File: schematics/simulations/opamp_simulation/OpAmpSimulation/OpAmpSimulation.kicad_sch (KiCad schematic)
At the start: 9 parts, among them U1 ${SIM.PARAMS}

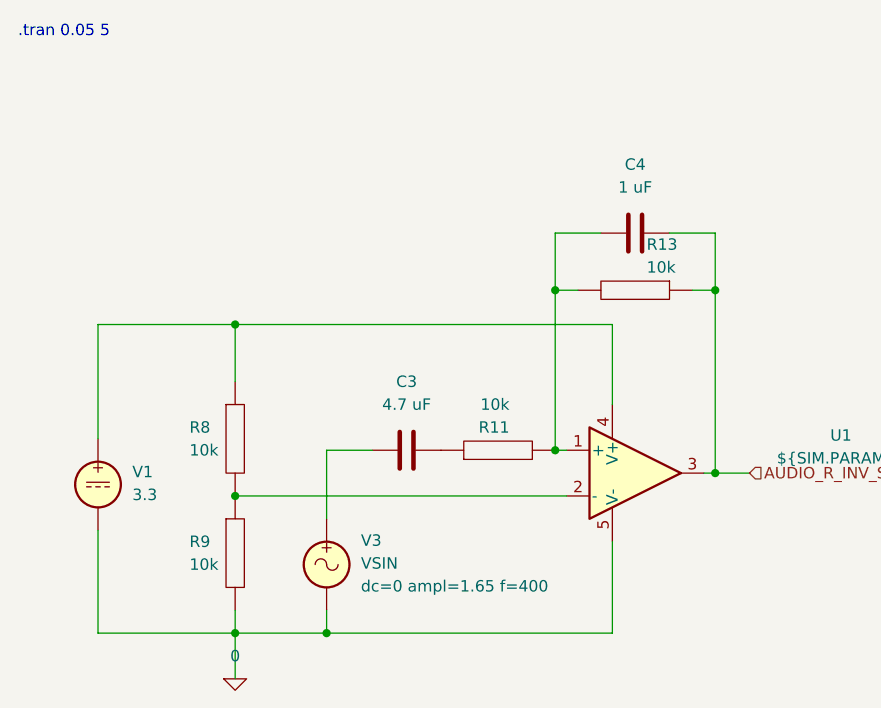
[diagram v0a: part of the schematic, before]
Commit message: [opamp_simulation:*] Bug | Confused inverting / non-inverting input
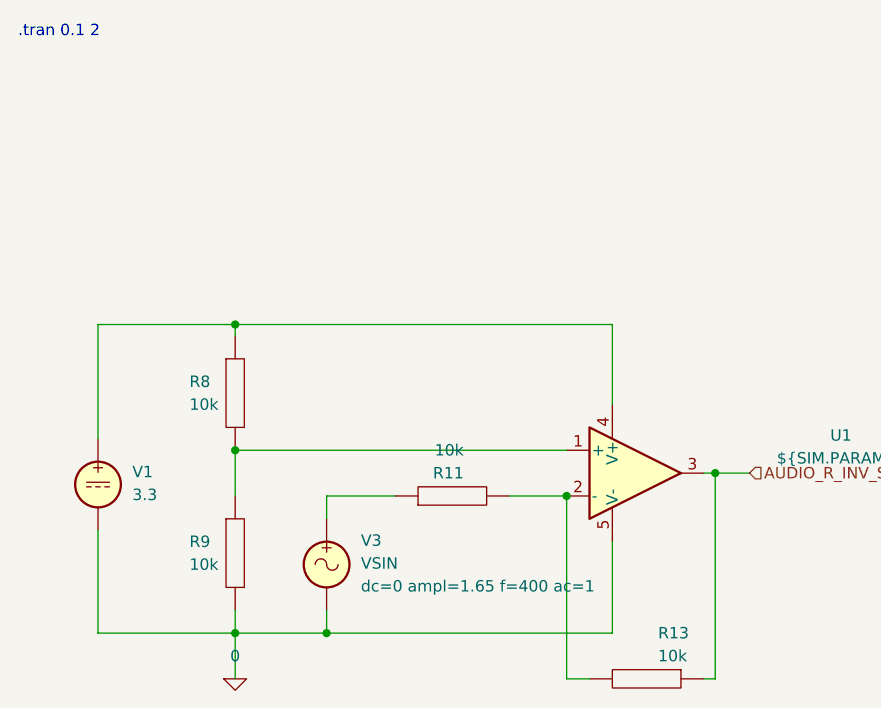
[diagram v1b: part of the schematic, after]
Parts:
- removed C3: 4.7 uF, symbol Device:C
- removed C4: 1 uF, symbol Device:C
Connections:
- net at V3.1: now also R11.1
- net at R11.2, R13.2: now also U1.2 (-); no longer U1.1 (+)
- net at R8.2, R9.1: now also U1.1 (+); no longer U1.2 (-)
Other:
- note added: ".tran 0.1 2"
- note removed: ".tran 0.05 5"
- moved on the sheet: R11, R13, R8
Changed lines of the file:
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@@
   (junction (at 68.58 166.37) (diameter 0) (color 0 0 0 0)
   )
-  (junction (at 93.98 128.27) (diameter 0) (color 0 0 0 0)
-  )
-  (junction (at 111.76 128.27) (diameter 0) (color 0 0 0 0)
-  )
-  (junction (at 93.98 146.05) (diameter 0) (color 0 0 0 0)
-  )
-  (junction (at 58.42 151.13) (diameter 0) (color 0 0 0 0)
+  (junction (at 58.42 146.05) (diameter 0) (color 0 0 0 0)
+  )
+  (junction (at 95.25 151.13) (diameter 0) (color 0 0 0 0)
   )
   (junction (at 58.42 132.08) (diameter 0) (color 0 0 0 0)
@@
   (junction (at 111.76 148.59) (diameter 0) (color 0 0 0 0)
   )
-  (wire (pts (xy 68.58 153.67) (xy 68.58 146.05))
+  (wire (pts (xy 68.58 153.67) (xy 68.58 151.13))
     (stroke (width 0) (type default))
   )
@@
     (stroke (width 0) (type default))
   )
-  (wire (pts (xy 111.76 128.27) (xy 111.76 148.59))
+  (wire (pts (xy 111.76 171.45) (xy 111.76 148.59))
     (stroke (width 0) (type default))
   )
@@
     (stroke (width 0) (type default))
   )
-  (wire (pts (xy 58.42 132.08) (xy 58.42 138.43))
+  (wire (pts (xy 58.42 132.08) (xy 58.42 133.35))
+    (stroke (width 0) (type default))
+  )
+  (wire (pts (xy 58.42 146.05) (xy 95.25 146.05))
+    (stroke (width 0) (type default))
+  )
+  (wire (pts (xy 88.9 151.13) (xy 95.25 151.13))
     (stroke (width 0) (type default))
   )
@@
     (stroke (width 0) (type default))
   )
-  (wire (pts (xy 106.68 121.92) (xy 111.76 121.92))
-    (stroke (width 0) (type default))
-  )
   (wire (pts (xy 43.18 132.08) (xy 58.42 132.08))
     (stroke (width 0) (type default))
@@
     (stroke (width 0) (type default))
   )
-  (wire (pts (xy 58.42 151.13) (xy 95.25 151.13))
-    (stroke (width 0) (type default))
-  )
-  (wire (pts (xy 68.58 146.05) (xy 73.66 146.05))
+  (wire (pts (xy 68.58 151.13) (xy 76.2 151.13))
     (stroke (width 0) (type default))
   )
@@
     (stroke (width 0) (type default))
   )
-  (wire (pts (xy 109.22 128.27) (xy 111.76 128.27))
+  (wire (pts (xy 110.49 171.45) (xy 111.76 171.45))
     (stroke (width 0) (type default))
   )
@@
     (stroke (width 0) (type default))
   )
-  (wire (pts (xy 93.98 121.92) (xy 93.98 128.27))
-    (stroke (width 0) (type default))
-  )
   (wire (pts (xy 68.58 166.37) (xy 58.42 166.37))
     (stroke (width 0) (type default))
@@
     (stroke (width 0) (type default))
   )
+  (wire (pts (xy 58.42 146.05) (xy 58.42 151.13))
+    (stroke (width 0) (type default))
+  )
   (wire (pts (xy 100.33 166.37) (xy 68.58 166.37))
     (stroke (width 0) (type default))
   )
-  (wire (pts (xy 99.06 121.92) (xy 93.98 121.92))
-    (stroke (width 0) (type default))
-  )
-  (wire (pts (xy 93.98 146.05) (xy 95.25 146.05))
-    (stroke (width 0) (type default))
-  )
-  (wire (pts (xy 111.76 121.92) (xy 111.76 128.27))
-    (stroke (width 0) (type default))
-  )
-  (wire (pts (xy 96.52 128.27) (xy 93.98 128.27))
+  (wire (pts (xy 95.25 171.45) (xy 95.25 151.13))
+    (stroke (width 0) (type default))
+  )
+  (wire (pts (xy 97.79 171.45) (xy 95.25 171.45))
     (stroke (width 0) (type default))
   )
@@
     (stroke (width 0) (type default))
   )
-  (wire (pts (xy 93.98 128.27) (xy 93.98 146.05))
-    (stroke (width 0) (type default))
-  )
-  (text ".tran 0.05 5" (at 34.29 100.33 0)
+  (text ".tran 0.1 2" (at 34.29 100.33 0)
     (effects (font (size 1.27 1.27)) (justify left bottom))
   )
@@
     )
   )
-  (symbol (lib_id "Device:C") (at 77.47 146.05 90) (unit 1)
-    (in_bom yes) (on_board yes) (dnp no) (fields_autoplaced)
-    (property "Reference" "C3" (at 77.47 138.43 90)
-      (effects (font (size 1.27 1.27)))
-    )
-    (property "Value" "4.7 uF" (at 77.47 140.97 90)
-      (effects (font (size 1.27 1.27)))
-    )
-    (property "Footprint" "" (at 81.28 145.0848 0)
-      (effects (font (size 1.27 1.27)) hide)
-    )
-    (property "Datasheet" "~" (at 77.47 146.05 0)
-      (effects (font (size 1.27 1.27)) hide)
-    )
-    (pin "1")
-    (pin "2")
-    (instances
-      (project "OpAmpSimulation"
-        (path "/0d0a973c-3ed5-4fec-a6a9-6f11d3a34d9a"
-          (reference "C3") (unit 1)
-        )
-      )
-      (project "stm32f030_adc"
-        (path "/85629656-c73b-4e1f-b8e8-4366f4b01266"
-          (reference "C11") (unit 1)
-        )
-        (path "/85629656-c73b-4e1f-b8e8-4366f4b01266/b4185304-bcce-4cb1-98f3-8bffc8e76c1e"
-          (reference "C11") (unit 1)
-        )
-      )
-    )
-  )
-  (symbol (lib_id "pspice:R") (at 87.63 146.05 90) (unit 1)
-    (in_bom yes) (on_board yes) (dnp no)
-    (property "Reference" "R11" (at 88.9 143.51 90)
-      (effects (font (size 1.27 1.27)) (justify left))
-    )
-    (property "Value" "10k" (at 88.9 140.97 90)
-      (effects (font (size 1.27 1.27)) (justify left))
-    )
-    (property "Footprint" "" (at 87.63 146.05 0)
-      (effects (font (size 1.27 1.27)) hide)
-    )
-    (property "Datasheet" "~" (at 87.63 146.05 0)
+  (symbol (lib_id "pspice:R") (at 82.55 151.13 90) (unit 1)
+    (in_bom yes) (on_board yes) (dnp no)
+    (property "Reference" "R11" (at 83.82 148.59 90)
+      (effects (font (size 1.27 1.27)) (justify left))
+    )
+    (property "Value" "10k" (at 83.82 146.05 90)
+      (effects (font (size 1.27 1.27)) (justify left))
+    )
+    (property "Footprint" "" (at 82.55 151.13 0)
+      (effects (font (size 1.27 1.27)) hide)
+    )
+    (property "Datasheet" "~" (at 82.55 151.13 0)
       (effects (font (size 1.27 1.27)) hide)
     )
@@
     )
   )
-  (symbol (lib_id "pspice:R") (at 58.42 144.78 0) (unit 1)
-    (in_bom yes) (on_board yes) (dnp no)
-    (property "Reference" "R8" (at 53.34 143.51 0)
-      (effects (font (size 1.27 1.27)) (justify left))
-    )
-    (property "Value" "10k" (at 53.34 146.05 0)
-      (effects (font (size 1.27 1.27)) (justify left))
-    )
-    (property "Footprint" "" (at 58.42 144.78 0)
-      (effects (font (size 1.27 1.27)) hide)
-    )
-    (property "Datasheet" "~" (at 58.42 144.78 0)
+  (symbol (lib_id "pspice:R") (at 58.42 139.7 0) (unit 1)
+    (in_bom yes) (on_board yes) (dnp no)
+    (property "Reference" "R8" (at 53.34 138.43 0)
+      (effects (font (size 1.27 1.27)) (justify left))
+    )
+    (property "Value" "10k" (at 53.34 140.97 0)
+      (effects (font (size 1.27 1.27)) (justify left))
+    )
+    (property "Footprint" "" (at 58.42 139.7 0)
+      (effects (font (size 1.27 1.27)) hide)
+    )
+    (property "Datasheet" "~" (at 58.42 139.7 0)
       (effects (font (size 1.27 1.27)) hide)
     )
@@
     )
   )
-  (symbol (lib_id "pspice:R") (at 102.87 128.27 270) (unit 1)
-    (in_bom yes) (on_board yes) (dnp no)
-    (property "Reference" "R13" (at 104.14 123.19 90)
-      (effects (font (size 1.27 1.27)) (justify left))
-    )
-    (property "Value" "10k" (at 104.14 125.73 90)
-      (effects (font (size 1.27 1.27)) (justify left))
-    )
-    (property "Footprint" "" (at 102.87 128.27 0)
-      (effects (font (size 1.27 1.27)) hide)
-    )
-    (property "Datasheet" "~" (at 102.87 128.27 0)
+  (symbol (lib_id "pspice:R") (at 104.14 171.45 270) (unit 1)
+    (in_bom yes) (on_board yes) (dnp no)
+    (property "Reference" "R13" (at 105.41 166.37 90)
+      (effects (font (size 1.27 1.27)) (justify left))
+    )
+    (property "Value" "10k" (at 105.41 168.91 90)
+      (effects (font (size 1.27 1.27)) (justify left))
+    )
+    (property "Footprint" "" (at 104.14 171.45 0)
+      (effects (font (size 1.27 1.27)) hide)
+    )
+    (property "Datasheet" "~" (at 104.14 171.45 0)
       (effects (font (size 1.27 1.27)) hide)
     )
@@
       (effects (font (size 1.27 1.27)) hide)
     )
-    (property "Sim.Params" "dc=0 ampl=1.65 f=400" (at 72.39 161.1602 0)
+    (property "Sim.Params" "dc=0 ampl=1.65 f=400 ac=1" (at 72.39 161.1602 0)
       (effects (font (size 1.27 1.27)) (justify left))
     )
@@
         (path "/85629656-c73b-4e1f-b8e8-4366f4b01266/b4185304-bcce-4cb1-98f3-8bffc8e76c1e"
           (reference "V3") (unit 1)
-        )
-      )
-    )
-  )
-  (symbol (lib_id "Device:C") (at 102.87 121.92 270) (unit 1)
-    (in_bom yes) (on_board yes) (dnp no)
-    (property "Reference" "C4" (at 102.87 114.3 90)
-      (effects (font (size 1.27 1.27)))
-    )
-    (property "Value" "1 uF" (at 102.87 116.84 90)
-      (effects (font (size 1.27 1.27)))
-    )
-    (property "Footprint" "" (at 99.06 122.8852 0)
-      (effects (font (size 1.27 1.27)) hide)
-    )
-    (property "Datasheet" "~" (at 102.87 121.92 0)
-      (effects (font (size 1.27 1.27)) hide)
-    )
-    (pin "1")
-    (pin "2")
-    (instances
-      (project "OpAmpSimulation"
-        (path "/0d0a973c-3ed5-4fec-a6a9-6f11d3a34d9a"
-          (reference "C4") (unit 1)
-        )
-      )
-      (project "stm32f030_adc"
-        (path "/85629656-c73b-4e1f-b8e8-4366f4b01266"
-          (reference "C12") (unit 1)
-        )
-        (path "/85629656-c73b-4e1f-b8e8-4366f4b01266/b4185304-bcce-4cb1-98f3-8bffc8e76c1e"
-          (reference "C12") (unit 1)
         )
       )
@@
   )
   (symbol (lib_id "Simulation_SPICE:OPAMP") (at 102.87 148.59 0) (unit 1)
-    (in_bom yes) (on_board yes) (dnp no) (fields_autoplaced)
+    (in_bom yes) (on_board yes) (dnp no)
     (property "Reference" "U1" (at 125.73 144.3991 0)
       (effects (font (size 1.27 1.27)))

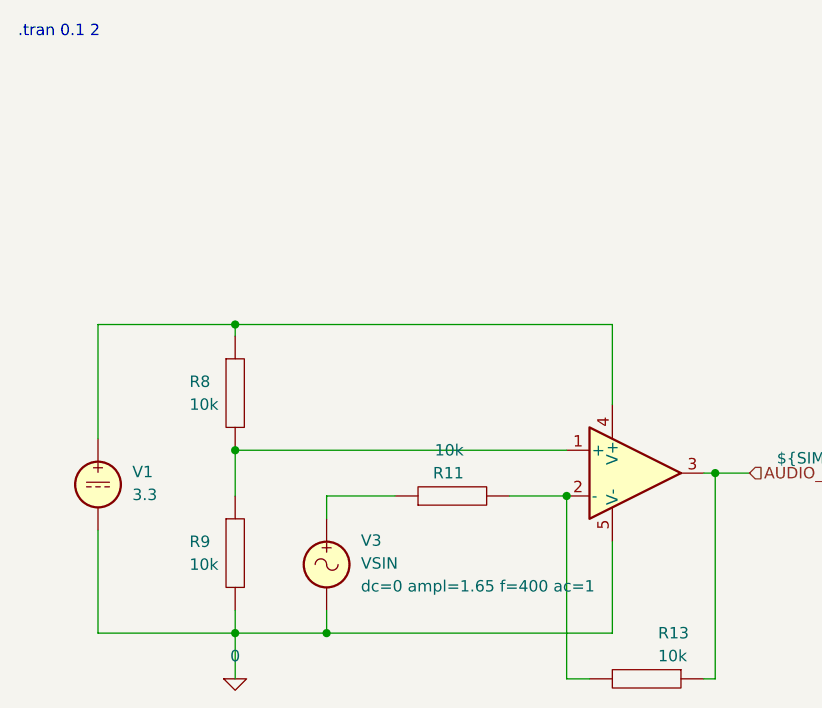
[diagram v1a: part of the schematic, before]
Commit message: [opamp_simulation:OpAmpSimulation] Enh | Adjusted simulation parameters
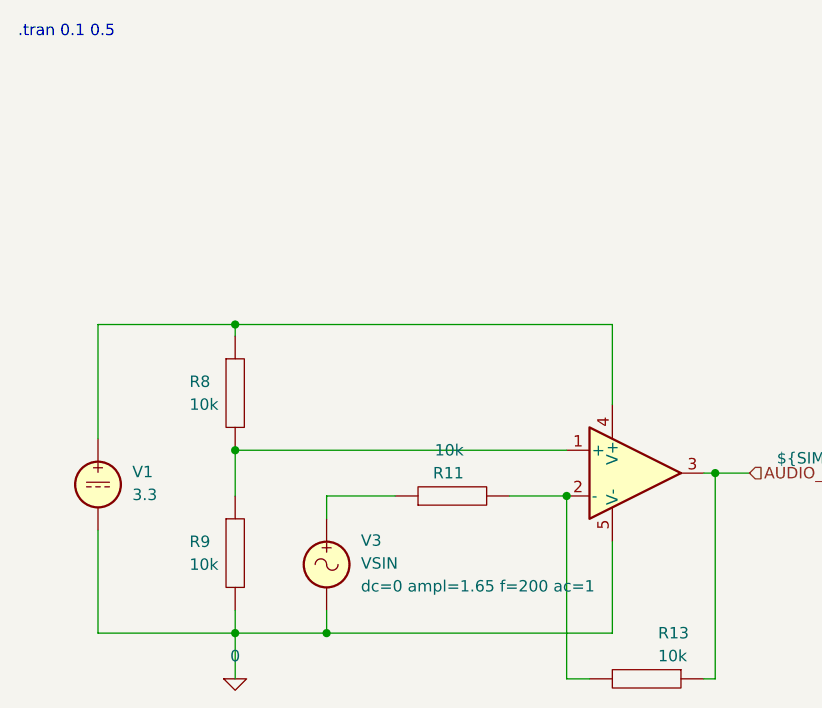
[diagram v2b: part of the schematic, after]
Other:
- note added: ".tran 0.1 0.5"
- note removed: ".tran 0.1 2"
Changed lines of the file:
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@@
     (stroke (width 0) (type default))
   )
-  (text ".tran 0.1 2" (at 34.29 100.33 0)
+  (text ".tran 0.1 0.5" (at 34.29 100.33 0)
     (effects (font (size 1.27 1.27)) (justify left bottom))
   )
@@
       (effects (font (size 1.27 1.27)) hide)
     )
-    (property "Sim.Params" "dc=0 ampl=1.65 f=400 ac=1" (at 72.39 161.1602 0)
+    (property "Sim.Params" "dc=0 ampl=1.65 f=200 ac=1" (at 72.39 161.1602 0)
       (effects (font (size 1.27 1.27)) (justify left))
     )
